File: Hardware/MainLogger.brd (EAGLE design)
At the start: 90 x 70 mm, 225 parts, among them J2 GEMS_POWER_PLUGINPUT, J4 U.FL, Q1 DMG3404, Q2 MOSFET_PCH-DMP3036SFG, Q3 MOSFET_PCH-DMP3036SFG, Q4 DMG3404, Q5 NX2301P, U1 MMC5633, U10 MXC6655, U11 FXMAR2102UMLP, U12 MCP79412SOIC, U13 SN74LVC1G17DCK, U14 FXMAR2102UMLP, U15 SN74AUP1G08DCK, U16 TPL5010DDC, U17 TPL5010DDC, U18 HALL_EFFECT_SI7201, U19 LP59073.3VYKE, U2 PAC1934QFN, U20 VEML3328, U21 MIC22602, U23 MB85RC, U24 SN74AUP3G34DCU, U25 SIP32431TDFN, U26 PAC1934QFN, U27 MCP23018QFN, U28 PCA9634QFN, U3 LTC4412S6, U4 BQ25616, U5 MCP23018QFN, U6 MAX-M8W, U7 B_SERIES_M.2EKEY_3042, U8 TCR2LE31ESV, U9 TPS61282D

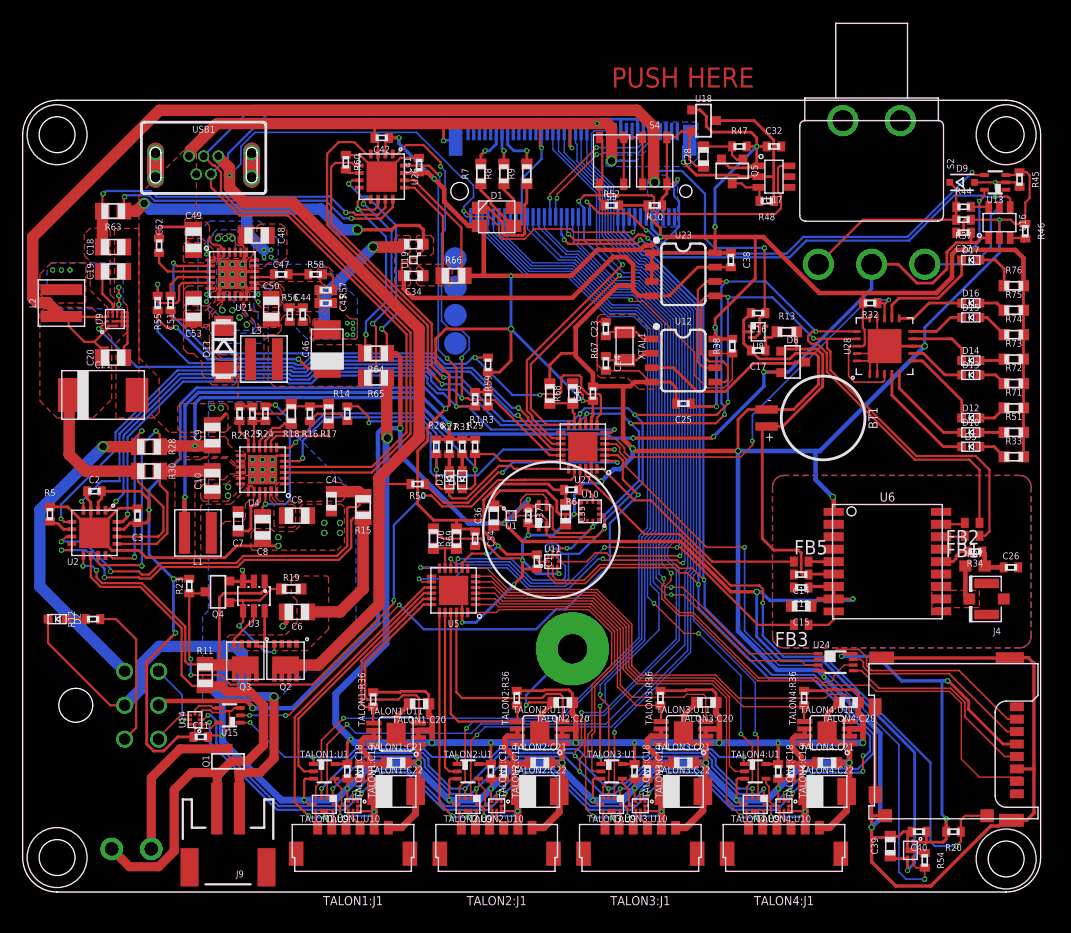
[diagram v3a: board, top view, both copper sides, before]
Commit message: Layout and cleanup complete, review required
Also add test points
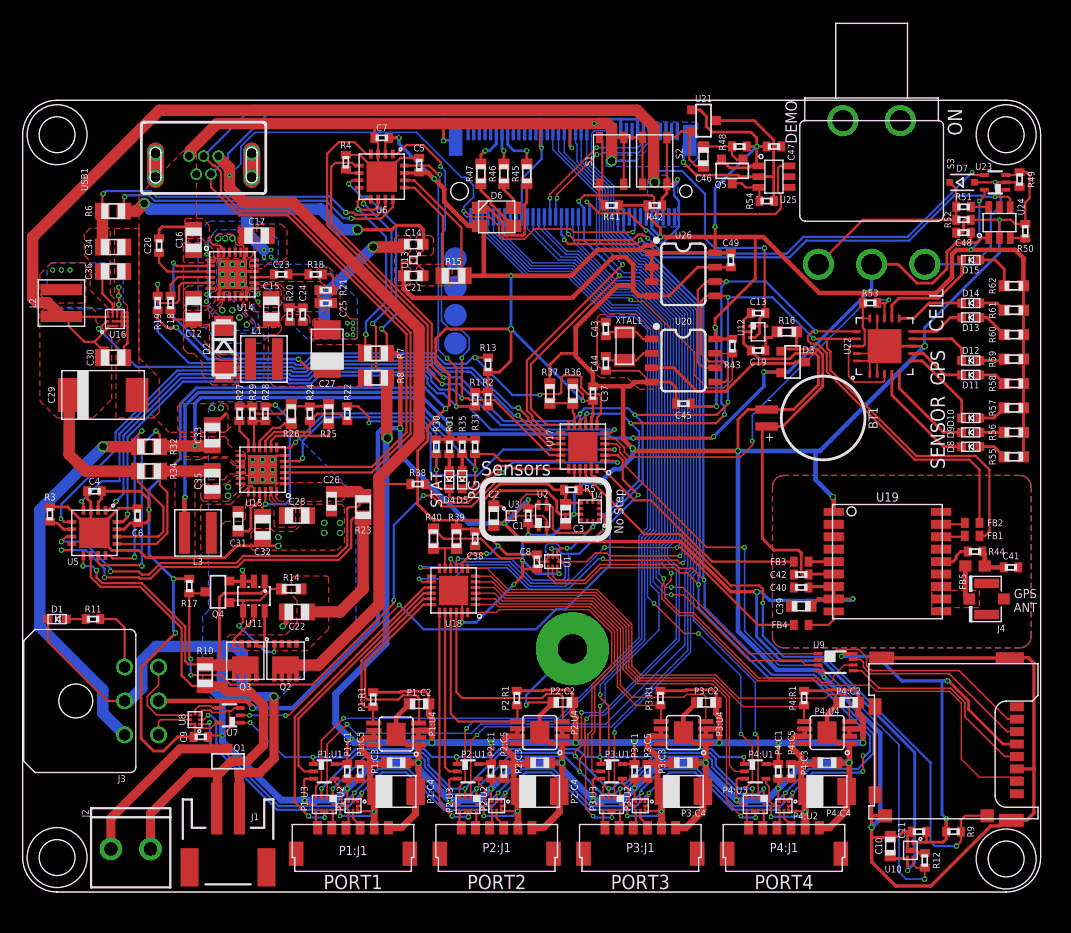
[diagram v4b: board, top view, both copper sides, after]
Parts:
- removed C50: 22uF, bschulz_passives:C0805
- removed C51: 1nF, bschulz_passives:C0402
- removed C52: 10nF, bschulz_passives:C0402
- removed C54: 0.1uF, bschulz_passives:C0402
- removed D16, D17: LED0603, bschulz:LED_0603
- removed FB7: 30Ω/1.8A, SparkFun-Coils:0603
- removed J9: (no value), bschulz:JST-2-SMD
- removed R63, R64, R65: 2m, bschulz_passives:R0805
- removed R66: 10m, bschulz_passives:R0805
- removed R67: (no value), bschulz_passives:R0603
- removed R71, R72, R73, R74: 220R, bschulz_passives:R0603
- removed S4: BUTTON4.2X3.2, bschulz:SWITCH_4.2X3.2
- removed U27: MCP23018QFN, bschulz:QFN24
- added $3_178_$_2021-10-08_21-38-43: B_SERIES_M.2EKEY_3042, Particle-Devices:PARTICLE_M.2EKEY
- added C22: 10uF, bschulz_passives:C0805
- added C29: 220uF, bschulz_passives:C2917
- added C30: 1.5uF, bschulz_passives:C0805
- added C31: 47nF, bschulz_passives:C0603
- added D7: BAT54WS, bschulz:SOD323-R
- added D8: LED0603, bschulz:LED_0603
- added FB4: (no value), bschulz:R0402
- added J3: GEMS_POWER_PLUGINPUT, bschulz:2X3_MICROFIT_RT
- added R2, R49: 1M, bschulz_passives:R0402
- added R22, R4: 0R, bschulz_passives:R0402
- added R35, R41, R42: 10k, bschulz_passives:R0402
- added R43, R53: 100k, bschulz_passives:R0402
- added S1: BUTTON4.2X3.2, bschulz:SWITCH_4.2X3.2
- C10: value 10uF -> 1uF; device bschulz_passives:C0805 -> bschulz_passives:C0603
- C14: value 0.1uF -> 1uF; device bschulz_passives:C0402 -> bschulz_passives:C0603
- C15: value 1uF -> 22uF; device bschulz_passives:C0603 -> bschulz_passives:C0805
- C16, C17: value 0.1uF -> 22uF; device bschulz_passives:C0402 -> bschulz_passives:C0805
- C18: value 10uF -> 1nF; device bschulz_passives:C0805 -> bschulz_passives:C0402
- C19, C5, C6, C9: value 10uF -> 0.1uF; device bschulz_passives:C0805 -> bschulz_passives:C0402
- C2, C3: value 0.1uF -> 2.2uF; device bschulz_passives:C0402 -> bschulz_passives:C0603
- C20: value 1.5uF -> 10nF; device bschulz_passives:C0805 -> bschulz_passives:C0402
- C21: value 220uF -> 1uF; device bschulz_passives:C2917 -> bschulz_passives:C0603
- C23: value 9pF -> 39pF
- C24: value 9pF -> 10nF
- C25: value 0.1uF -> 100pF
- C26: value 47pF -> 1uF; device bschulz_passives:C0402 -> bschulz_passives:C0603
- C27: value 0.1uF -> 100uF; device bschulz_passives:C0402 -> bschulz_passives:C1411_TANT
- C28, C33, C34: value 1uF -> 10uF; device bschulz_passives:C0603 -> bschulz_passives:C0805
- C32: value 0.1uF -> 4.7uF; device bschulz_passives:C0402 -> bschulz_passives:C0805
- C35, C36: value 2.2uF -> 10uF; device bschulz_passives:C0603 -> bschulz_passives:C0805
- C4: value 1uF -> 0.1uF; device bschulz_passives:C0603 -> bschulz_passives:C0402
- C41: value 0.1uF -> 47pF
- C43: value 0.1uF -> 9pF
- C44: value 10nF -> 9pF
- C45: value 100pF -> 0.1uF
- C46: value 100uF -> 1uF; device bschulz_passives:C1411_TANT -> bschulz_passives:C0603
- C47: value 39pF -> 0.1uF
- C48, C49: value 22uF -> 0.1uF; device bschulz_passives:C0805 -> bschulz_passives:C0402
- C7: value 47nF -> 0.1uF; device bschulz_passives:C0603 -> bschulz_passives:C0402
- C8: value 4.7uF -> 0.1uF; device bschulz_passives:C0805 -> bschulz_passives:C0402
- D1: value CLVBA-FKA -> LED0603; device bschulz:CLVBA-FKA -> bschulz:LED_0603
- D11: value CDBA3100 -> LED0603; device bschulz:DO214AC -> bschulz:LED_0603
- D2: value LED0603 -> CDBA3100; device bschulz:LED_0603 -> bschulz:DO214AC
- D3: value LED0603 -> BAT54C; device bschulz:LED_0603 -> bschulz:SOT23-3
- D6: value BAT54C -> CLVBA-FKA; device bschulz:SOT23-3 -> bschulz:CLVBA-FKA
- D9: value BAT54WS -> LED0603; device bschulz:SOD323-R -> bschulz:LED_0603
- FB5: value (none) -> 30Ω/1.8A; device bschulz:R0402 -> SparkFun-Coils:0603
- J1: device bschulz:SCREWTERMINAL-3.5MM-2_ROUND_RESTRICT -> bschulz:JST-2-SMD
- J2: value GEMS_POWER_PLUGINPUT -> (none); device bschulz:2X3_MICROFIT_RT -> bschulz:SCREWTERMINAL-3.5MM-2_ROUND_RESTRICT
- L1: value 1uH -> 1uF
- L3: value 1uF -> 1uH
- R10, R6: value 10k -> 2m; device bschulz_passives:R0402 -> bschulz_passives:R0805
- R11: value 2m -> 1k; device bschulz_passives:R0805 -> bschulz_passives:R0402
- R12: value 1k -> 100k
- R13: value 1k -> 100k; device bschulz_passives:R0603 -> bschulz_passives:R0402
- R14: value 0R -> 470k; device bschulz_passives:R0402 -> bschulz_passives:R0603
- R15: value 2m -> 10m
- R16: value 1M -> 1k; device bschulz_passives:R0402 -> bschulz_passives:R0603
- R17: value 470R -> 1M; device bschulz_passives:R0603 -> bschulz_passives:R0402
- R18: value 220R -> 20k; device bschulz_passives:R0603 -> bschulz_passives:R0402
- R19: value 470k -> 100k; device bschulz_passives:R0603 -> bschulz_passives:R0402
- R20, R54: value 100k -> 10k
- R21: value 10k -> 2.7k
- R23: value 1M -> 2m; device bschulz_passives:R0402 -> bschulz_passives:R0805
- R24, R38: value 100k -> 1M
- R25: value 100k -> 470R; device bschulz_passives:R0402 -> bschulz_passives:R0603
- R26: value 1M -> 220R; device bschulz_passives:R0402 -> bschulz_passives:R0603
- R28: value 10m -> 100k; device bschulz_passives:R0805 -> bschulz_passives:R0402
- R29, R50: value 1M -> 100k
- R3: value 1M -> 0R
- R30: value 10m -> 1M; device bschulz_passives:R0805 -> bschulz_passives:R0402
- R32: value 100k -> 10m; device bschulz_passives:R0402 -> bschulz_passives:R0805
- R33: value 220R -> 1M; device bschulz_passives:R0603 -> bschulz_passives:R0402
- R34: value 10 -> 10m; device bschulz_passives:R0402 -> bschulz_passives:R0805
- R37: value 1M -> (none); device bschulz_passives:R0402 -> bschulz_passives:R0603
- R44: value 10k -> 10
- R45: value 1M -> 4.7k; device bschulz_passives:R0402 -> bschulz_passives:R0603
- R46, R47: value 100k -> 4.7k; device bschulz_passives:R0402 -> bschulz_passives:R0603
- R48: value 10k -> 100k
- R5: value 0R -> 10k
- R51: value 220R -> 10k; device bschulz_passives:R0603 -> bschulz_passives:R0402
- R52: value 10k -> 1M
- R55, R59: value 100k -> 220R; device bschulz_passives:R0402 -> bschulz_passives:R0603
- R56: value 10k -> 220R; device bschulz_passives:R0402 -> bschulz_passives:R0603
- R57: value 2.7k -> 220R; device bschulz_passives:R0402 -> bschulz_passives:R0603
- R58: value 20k -> 220R; device bschulz_passives:R0402 -> bschulz_passives:R0603
- R60: value 0R -> 220R; device bschulz_passives:R0402 -> bschulz_passives:R0603
- R7, R8: value 4.7k -> 2m; device bschulz_passives:R0603 -> bschulz_passives:R0805
- R9: value 4.7k -> 100k; device bschulz_passives:R0603 -> bschulz_passives:R0402
- S2: value SPDT7103K2CWA -> BUTTON4.2X3.2; device bschulz:7103K2CWA -> bschulz:SWITCH_4.2X3.2
- S3: value BUTTON4.2X3.2 -> SPDT7103K2CWA; device bschulz:SWITCH_4.2X3.2 -> bschulz:7103K2CWA
- U1: value MMC5633 -> FXMAR2102UMLP; device bschulz:BGA_4 -> bschulz:UQFN-8_1.4X1.2
- U10: value MXC6655 -> SIP32431TDFN; device bschulz:LGA-12_2X2 -> bschulz:TDFN_4
- U11: value FXMAR2102UMLP -> LTC4412S6; device bschulz:UQFN-8_1.4X1.2 -> bschulz:SOT23-6L
- U12: value MCP79412SOIC -> TCR2LE31ESV; device bschulz:SO08 -> bschulz:SOT-553
- U13: value SN74LVC1G17DCK -> LP59073.3VYKE; device bschulz:DCK_R-PDSO-G5 -> bschulz:YKE0004
- U14: value FXMAR2102UMLP -> MIC22602; device bschulz:UQFN-8_1.4X1.2 -> bschulz:QFN24_POWER
- U15: value SN74AUP1G08DCK -> BQ25616; device bschulz:DCK_R-PDSO-G5 -> bschulz:QFN24_POWER
- U16: value TPL5010DDC -> TPS61282D; device bschulz:DDC_R-PDSO-G6 -> bschulz:YFP0016
- U17: value TPL5010DDC -> MCP23018QFN; device bschulz:DDC_R-PDSO-G6 -> bschulz:QFN24
- U18: value HALL_EFFECT_SI7201 -> MCP23018QFN; device bschulz:SOT23-3 -> bschulz:QFN24
- U19: value LP59073.3VYKE -> MAX-M8W; device bschulz:YKE0004 -> bschulz:MAX-M8
- U2: value PAC1934QFN -> VEML3328; device bschulz:QFN16 -> bschulz:VEML6075
- U20: value VEML3328 -> MCP79412SOIC; device bschulz:VEML6075 -> bschulz:SO08
- U21: value MIC22602 -> HALL_EFFECT_SI7201; device bschulz:QFN24_POWER -> bschulz:SOT23-3
- U23: value MB85RC -> SN74LVC1G17DCK; device bschulz:SO08 -> bschulz:DCK_R-PDSO-G5
- U24: value SN74AUP3G34DCU -> TPL5010DDC; device bschulz:DCU_(R-PDSO-G8) -> bschulz:DDC_R-PDSO-G6
- U25: value SIP32431TDFN -> TPL5010DDC; device bschulz:TDFN_4 -> bschulz:DDC_R-PDSO-G6
- U26: value PAC1934QFN -> MB85RC; device bschulz:QFN16 -> bschulz:SO08
- U3: value LTC4412S6 -> MMC5633; device bschulz:SOT23-6L -> bschulz:BGA_4
- U4: value BQ25616 -> MXC6655; device bschulz:QFN24_POWER -> bschulz:LGA-12_2X2
- U5: value MCP23018QFN -> PAC1934QFN; device bschulz:QFN24 -> bschulz:QFN16
- U6: value MAX-M8W -> PAC1934QFN; device bschulz:MAX-M8 -> bschulz:QFN16
- U7: value B_SERIES_M.2EKEY_3042 -> SN74AUP1G08DCK; device Particle-Devices:PARTICLE_M.2EKEY -> bschulz:DCK_R-PDSO-G5
- U8: value TCR2LE31ESV -> FXMAR2102UMLP; device bschulz:SOT-553 -> bschulz:UQFN-8_1.4X1.2
- U9: value TPS61282D -> SN74AUP3G34DCU; device bschulz:YFP0016 -> bschulz:DCU_(R-PDSO-G8)
- moved U16 78.7 mm to (8.16, 50.7), turned to 90 degrees
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- renumbered C53 to C12, R68 to R36, R69 to R40, R70 to R39, R75 to R61, R76 to R62, SD2 to SD1, TALON1:C18 to P1:C1, TALON1:C19 to P1:C5, TALON1:C20 to P1:C2, TALON1:C21 to P1:C3, TALON1:C22 to P1:C4, TALON1:J1 to P1:J1, TALON1:R36 to P1:R1, TALON1:U1 to P1:U1, TALON1:U10 to P1:U2, TALON1:U11 to P1:U4, TALON1:U9 to P1:U3, TALON2:C18 to P2:C1, TALON2:C19 to P2:C5, TALON2:C20 to P2:C2, TALON2:C21 to P2:C3, TALON2:C22 to P2:C4, TALON2:J1 to P2:J1, TALON2:R36 to P2:R1, TALON2:U1 to P2:U1, TALON2:U10 to P2:U2, TALON2:U11 to P2:U4, TALON2:U9 to P2:U3, TALON3:C18 to P3:C1, TALON3:C19 to P3:C5, TALON3:C20 to P3:C2, TALON3:C21 to P3:C3, TALON3:C22 to P3:C4, TALON3:J1 to P3:J1, TALON3:R36 to P3:R1, TALON3:U1 to P3:U1, TALON3:U10 to P3:U2, TALON3:U11 to P3:U4, TALON3:U9 to P3:U3, TALON4:C18 to P4:C1, TALON4:C19 to P4:C5, TALON4:C20 to P4:C2, TALON4:C21 to P4:C3, TALON4:C22 to P4:C4, TALON4:J1 to P4:J1, TALON4:R36 to P4:R1, TALON4:U1 to P4:U1, TALON4:U10 to P4:U2, TALON4:U11 to P4:U4, TALON4:U9 to P4:U3, U28 to U22
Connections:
- net TALON1:3V3_TALON renamed P1:3V3_TALON
- net TALON1:I2C_EN_LOCAL renamed P1:I2C_EN_LOCAL
- net TALON1:RX_TALON renamed P1:RX_TALON
- net TALON1:SCL_EXT renamed P1:SCL_EXT
- net TALON1:SDA_EXT renamed P1:SDA_EXT
- net TALON1:TX_TALON renamed P1:TX_TALON
- net TALON2:3V3_TALON renamed P2:3V3_TALON
- net TALON2:I2C_EN_LOCAL renamed P2:I2C_EN_LOCAL
- net TALON2:RX_TALON renamed P2:RX_TALON
- net TALON2:SCL_EXT renamed P2:SCL_EXT
- net TALON2:SDA_EXT renamed P2:SDA_EXT
- net TALON2:TX_TALON renamed P2:TX_TALON
- net TALON3:3V3_TALON renamed P3:3V3_TALON
- net TALON3:I2C_EN_LOCAL renamed P3:I2C_EN_LOCAL
- net TALON3:RX_TALON renamed P3:RX_TALON
- net TALON3:SCL_EXT renamed P3:SCL_EXT
- net TALON3:SDA_EXT renamed P3:SDA_EXT
- net TALON3:TX_TALON renamed P3:TX_TALON
- net TALON4:3V3_TALON renamed P4:3V3_TALON
- net TALON4:I2C_EN_LOCAL renamed P4:I2C_EN_LOCAL
- net TALON4:RX_TALON renamed P4:RX_TALON
- net TALON4:SCL_EXT renamed P4:SCL_EXT
- net TALON4:SDA_EXT renamed P4:SDA_EXT
- net TALON4:TX_TALON renamed P4:TX_TALON
- removed net N$20 (its old number): D3.ANODE, R27.1
- new net N$18: D5.ANODE, R35.1
- net !CE: now also R22.1, U17.3; no longer R14.1, U27.3
- net !CHG_PG: now also D5.CATHODE, R33.1, U15.7, U17.18; no longer D4.CATHODE, R29.1, U27.18, U4.7
- net !MODE: now also $3_178_$_2021-10-08_21-38-43.32, C46.1, R42.1, S2.1, S2.2, U21.2; no longer C28.1, R10.1, S4.1, S4.2, U18.2, U7.32
- net !RESET: now also $3_178_$_2021-10-08_21-38-43.34, FB4.2, R41.1, S1.1, S1.2, U17.12, U18.12, U25.6; no longer FB3.2, R52.1, S3.1, S3.2, U17.6, U27.12, U5.12, U7.34
- net !TALON1_FAULT: now also U18.17; no longer U5.17
- net !TALON2_FAULT: now also U18.21; no longer U5.21
- net !TALON3_FAULT: now also U18.2; no longer U5.2
- net !TALON4_FAULT: now also U18.6; no longer U5.6
- net 3V3_AUX: now also C1.1, C10.1, C2.1, C40.1, J3.5, R7.1, U10.3, U19.7, U19.8, U2.4, U3.B1; no longer C13.1, C15.1, C36.1, C37.1, J2.5, R64.1, U1.B1, U20.4, U25.3, U26.7, U6.8
- net 3V3_AUX_EN: now also R13.1, U14.2, U17.7; no longer R59.1, U21.2, U27.7
- net 3V3_AUX_PG: now also R19.1, U14.5, U17.15; no longer R55.1, U21.5, U27.15
- net 3V3_BULK: now also R8.1, U6.9; no longer R65.1, U26.9
- net 3V3_BULK+: now also C24.1, C27.ANODE, L1.P$2, R19.2, R20.2, R7.2, R8.2, U6.10, U6.8; no longer C44.1, C46.ANODE, L3.P$2, R55.2, R56.2, R64.2, R65.2, U26.10, U26.8
- net 3V3_CORE: now also $3_178_$_2021-10-08_21-38-43.10, $3_178_$_2021-10-08_21-38-43.12, C37.1, C4.1, C45.1, C47.1, C49.1, C5.1, C6.1, C7.1, C8.1, C9.1, D6.2, R13.2, R15.2, R17.2, R2.2, R41.2, R42.2, R43.2, R48.2, R5.2, R53.2, R55.2, R56.2, R57.2, R58.2, R60.2, U1.1, U1.8, U17.8, U18.8, U20.8, U21.1, U23.5, U25.1, U26.1, U26.3, U26.8, U4.7, U5.15, U5.2, U6.14, U6.15, U6.2, U7.5, U8.1, U8.8; no longer C1.1, C11.1, C2.1, C25.1, C32.1, C35.1, C41.1, C42.1, C43.1, C54.1, D1.2, R10.2, R23.2, R3.2, R32.2, R33.2, R38.2, R47.2, R51.2, R52.2, R6.2, R66.2, R71.2, R72.2, R73.2, R74.2, U10.7, U11.1, U11.8, U12.8, U13.5, U14.1, U14.8, U15.5, U17.1, U18.1, U2.15, U2.2, U23.1, U23.2, U23.3, U23.8, U26.14, U26.15, U27.8, U5.8, U7.10, U7.12
- net 3V3_CORE+: now also C21.1, R15.1, U13.A2, U6.13; no longer C34.1, R66.1, U19.A2, U26.13
- net 3V3_SD: now also C11.1, R9.2, U10.1, U9.8; no longer C40.1, R20.2, U24.8, U25.1
- net 3V3_SD_EN: now also R12.2, U10.4, U17.4; no longer R54.2, U25.4, U27.4
- net ACCEL_INT: now also R5.1, U17.21, U4.5; no longer R6.1, U10.5, U27.21
- net ANT_VCC: now also C41.1, FB5.2, R44.1; no longer C26.1, FB7.2, R34.1
- net BAT: now also J3.1, R32.2, U5.12; no longer J2.1, R28.2, U2.12
- net BAT_CHG: now also C33.1, C48.1, D3.2, R32.1, S3.2, U15.13, U15.14, U24.1, U5.11; no longer C27.1, C9.1, D6.2, R28.1, S2.2, U16.1, U2.11, U4.13, U4.14
- net BCKP_GPS: now also C42.1, D3.1, R16.2, U19.6; no longer C14.1, D6.1, R13.2, U6.6
- net BCKP_RTC: now also D3.3, U20.3; no longer D6.3, U12.3
- net BTST: now also C31.2, U15.21; no longer C7.2, U4.21
- net CHG_SOURCE: now also R17.1, U17.20; no longer R23.1, U27.20
- net CHG_STAT: now also D4.CATHODE, R30.1, U15.5, U17.19; no longer D3.CATHODE, R26.1, U27.19, U4.5
- net COMP: now also C23.1, U14.15; no longer C47.1, U21.15
- net CSA_ALERT: now also R2.1, U17.17, U5.1, U6.1; no longer R3.1, U2.1, U26.1, U27.17
- net CSA_EN: now also U17.6, U5.16, U6.16; no longer U2.16, U26.16, U27.6
- net D+: now also $3_178_$_2021-10-08_21-38-43.11, $3_178_$_2021-10-08_21-38-43.44, U15.3; no longer U4.3, U7.11, U7.44
- net D-: now also $3_178_$_2021-10-08_21-38-43.13, $3_178_$_2021-10-08_21-38-43.46, U15.4; no longer U4.4, U7.13, U7.46
- net DELAY: now also C20.1, U14.3; no longer C52.1, U21.3
- net EN_MAIN: now also R51.2, U24.6; no longer R44.2, U16.6
- net FAULT_BUS: now also D1.ANODE, R11.2; no longer D2.ANODE, R12.2
- net FB: now also C24.2, C25.1, R20.1, R21.2, U14.14; no longer C44.2, C45.1, R56.1, R57.2, U21.14
- net GND: now also $3_178_$_2021-10-08_21-38-43.1, $3_178_$_2021-10-08_21-38-43.15, $3_178_$_2021-10-08_21-38-43.21, $3_178_$_2021-10-08_21-38-43.3, $3_178_$_2021-10-08_21-38-43.39, $3_178_$_2021-10-08_21-38-43.49, $3_178_$_2021-10-08_21-38-43.5, $3_178_$_2021-10-08_21-38-43.56, $3_178_$_2021-10-08_21-38-43.7, $3_178_$_2021-10-08_21-38-43.76, $3_178_$_2021-10-08_21-38-43.77, $3_178_$_2021-10-08_21-38-43.9, $3_178_$_2021-10-08_21-38-43.GND, C21.2, C22.2, C27.CATHODE, C28.2, C29.-, C30.2, C44.2, C47.2, C7.2, D1.CATHODE, D2.A, J1.1, J3.2, R12.1, R21.1, R24.1, R26.1, R27.2, R29.1, R3.1, R4.1, R49.1, R50.1, R52.1, S1.3, S1.4, S2.3, S2.4, U1.4, U10.2, U10.EP, U11.2, U11.3, U12.2, U13.B2, U14.12, U14.16, U14.19, U14.24, U14.7, U14.EP, U14.EP@1, U14.EP@2, U14.EP@3, U14.EP@4, U14.EP@5, U14.EP@6, U14.EP@7, U14.EP@8, U14.EP@9, U15.17, U15.18, U15.6, U15.EP, U15.EP@1, U15.EP@2, U15.EP@3, U15.EP@4, U15.EP@5, U15.EP@6, U15.EP@7, U15.EP@8, U15.EP@9, U16.B2, U16.C2, U16.D1, U16.D2, U16.D3, U16.D4, U17.23, U17.EP, U18.23, U18.EP, U19.1, U19.10, U19.12, U19.15, U2.1, U20.4, U21.3, U23.3, U24.2, U26.4, U26.7, U3.A1, U4.9, U5.3, U6.3, U6.EP, U8.4, U9.4; no longer C21.-, C23.2, C24.2, C27.2, C46.CATHODE, C50.2, C51.2, C52.2, C54.2, D11.A, D2.CATHODE, J2.2, J9.1, R16.1, R17.1, R21.2, R45.1, R46.1, R48.1, R5.1, R57.1, R58.1, R60.1, R67.1, S3.3, S3.4, S4.3, S4.4, U1.A1, U10.9, U11.4, U12.4, U13.3, U14.4, U15.3, U16.2, U17.2, U18.3, U19.B2, U2.3, U2.EP, U20.1, U21.12, U21.16, U21.19, U21.24, U21.7, U21.EP, U21.EP@1, U21.EP@2, U21.EP@3, U21.EP@4, U21.EP@5, U21.EP@6, U21.EP@7, U21.EP@8, U21.EP@9, U23.4, U23.7, U24.4, U25.EP, U26.3, U26.EP, U27.23, U27.EP, U3.2, U3.3, U4.17, U4.18, U4.6, U4.EP, U4.EP@1, U4.EP@2, U4.EP@3, U4.EP@4, U4.EP@5, U4.EP@6, U4.EP@7, U4.EP@8, U4.EP@9, U5.23, U6.1, U6.10, U6.12, U6.15, U7.1, U7.15, U7.21, U7.39, U7.49, U7.5, U7.56, U7.7, U7.76, U7.77, U7.9, U7.GND, U8.2, U9.B2, U9.C2, U9.D1, U9.D2, U9.D3, U9.D4
- net GPS_ANT: now also FB5.1, U19.11; no longer FB7.1, U6.11
- net GPS_INT: now also FB3.1, U17.24; no longer FB5.1, U27.24
- net GPS_INT_CLEAN: now also FB3.2, U19.5; no longer FB5.2, U6.5
- net I2C_EXT_EN: now also U17.2, U7.2; no longer U15.2, U27.2
- net I2C_EXT_EN_OUT: now also U7.4, U8.5; no longer U14.5, U15.4
- net I2C_GLOBAL_EN: now also $3_178_$_2021-10-08_21-38-43.64, U7.1; no longer U15.1, U7.64
- net I2C_OB_EN: now also $3_178_$_2021-10-08_21-38-43.45, U1.5; no longer U11.5, U7.45
- net ICHG: now also R26.2, U15.10; no longer R18.2, U4.10
- net ILIM: now also R25.2, U15.8; no longer R17.2, U4.8
- net LED_BLUE: now also $3_178_$_2021-10-08_21-38-43.65, R47.2; no longer R7.2, U7.65
- net LED_EN: now also R53.1, U17.5; no longer R32.1, U27.5
- net LED_GREEN: now also $3_178_$_2021-10-08_21-38-43.63, R46.2; no longer R8.2, U7.63
- net LED_RED: now also $3_178_$_2021-10-08_21-38-43.61, R45.2; no longer R9.2, U7.61
- net MISO: now also $3_178_$_2021-10-08_21-38-43.50; no longer U7.50
- net MOSI: now also $3_178_$_2021-10-08_21-38-43.52, U9.1; no longer U24.1, U7.52
- net MOSI_BUF: now also U9.7; no longer U24.7
- net N$1: now also R3.2, U5.6; no longer R5.2, U2.6
- net N$10: now also R22.2, R24.2, U15.9; no longer R14.2, R16.2, U4.9
- net N$12: now also D7.A, R49.2, S3.3, U23.2; no longer D9.A, R45.2, S2.3, U13.2
- net N$13: now also C46.2, R48.1; no longer C28.2, R47.1
- net N$15: now also R38.1, U17.1; no longer R50.1, U27.1
- net N$17: now also R4.2, U6.6; no longer R60.2, U26.6
- net N$21: now also D6.3, R47.1; no longer D1.3, R7.1
- net N$22: now also D6.4, R46.1; no longer D1.4, R8.1
- net N$23: now also D6.1, R45.1; no longer D1.1, R9.1
- net N$24: now also FB4.1, U19.9; no longer FB3.1, U6.9
- net N$25: now also J3.3, R11.1; no longer J2.3, R12.1
- net N$29: now also D7.C, R51.1, R52.2, S3.1; no longer D9.C, R37.2, R44.1, S2.1
- net N$3: now also C19.1, R16.1, U12.4; no longer C17.1, R13.1, U8.4
- net N$30: now also R50.2, U24.3; no longer R46.2, U16.3
- net N$32: now also R54.2, U25.3; no longer R48.2, U17.3
- net N$33: now also C23.2, R18.2; no longer C47.2, R58.2
- net N$35: now also U18.11; no longer U5.11
- net N$36: now also D8.CATHODE; no longer D5.CATHODE
- net N$37: now also D9.CATHODE; no longer D10.CATHODE
- net N$38: now also R37.2, U17.11; no longer R67.2, U27.11
- net N$39: now also D10.CATHODE; no longer D12.CATHODE
- net N$4: now also C43.1, U20.1; no longer C23.1, U12.1
- net N$40: now also D11.CATHODE; no longer D13.CATHODE
- net N$41: now also D12.CATHODE; no longer D14.CATHODE
- net N$42: now also D13.CATHODE; no longer D15.CATHODE
- net N$43: now also D14.CATHODE; no longer D16.CATHODE
- net N$44: now also D15.CATHODE; no longer D17.CATHODE
- net N$45: now also D8.ANODE, R55.1; no longer D5.ANODE, R33.1
- net N$46: now also D9.ANODE, R56.1; no longer D10.ANODE, R51.1
- net N$47: now also D10.ANODE, R57.1; no longer D12.ANODE, R71.1
- net N$48: now also D11.ANODE, R58.1; no longer D13.ANODE, R72.1
- net N$49: now also D12.ANODE, R59.1; no longer D14.ANODE, R73.1
- net N$5: now also U11.5; no longer U3.5
- net N$50: now also D13.ANODE, R60.1; no longer D15.ANODE, R74.1
- net N$51: now also D14.ANODE; no longer D16.ANODE
- net N$52: now also D15.ANODE; no longer D17.ANODE
- net N$7: now also C44.1, U20.2; no longer C24.1, U12.2
- net OB_INT: now also $3_178_$_2021-10-08_21-38-43.43, U17.14; no longer U27.14, U7.43
- net PMID: now also C28.1, U15.23; no longer C5.1, U4.23
- net RC: now also C18.1, U14.4; no longer C51.1, U21.4
- net REGN: now also C32.1, R28.2, U15.22; no longer C8.1, R24.2, U4.22
- net RTC_INT: now also $3_178_$_2021-10-08_21-38-43.62, R43.1, U20.7; no longer R38.1, U12.7, U7.62
- net RX: now also $3_178_$_2021-10-08_21-38-43.38; no longer U7.38
- net SCK: now also $3_178_$_2021-10-08_21-38-43.54, U9.3; no longer U24.3, U7.54
- net SCK_BUF: now also U9.5; no longer U24.5
- net SCL: now also $3_178_$_2021-10-08_21-38-43.20, U1.3, U8.3; no longer U11.3, U14.3, U7.20
- net SCL_EXT: now also J3.6, U8.6; no longer J2.6, U14.6
- net SCL_GPS: now also U19.17; no longer U6.17
- net SCL_OB: now also U1.6, U17.9, U18.9, U2.3, U20.6, U26.6, U3.A2, U4.12, U5.4, U6.4; no longer U1.A2, U10.12, U11.6, U12.6, U2.4, U20.3, U23.6, U26.4, U27.9, U5.9
- net SDA: now also $3_178_$_2021-10-08_21-38-43.22, U1.2, U8.2; no longer U11.2, U14.2, U7.22
- net SDA_EXT: now also J3.4, U8.7; no longer J2.4, U14.7
- net SDA_GPS: now also U19.16; no longer U6.16
- net SDA_OB: now also U1.7, U17.10, U18.10, U2.2, U20.5, U3.B2, U4.2, U5.5, U6.5; no longer U1.B2, U10.2, U11.7, U12.5, U2.5, U20.2, U23.5, U27.10, U5.10
- net SD_CD: now also R9.1, U17.22; no longer R20.1, U27.22
- net SD_CS: now also $3_178_$_2021-10-08_21-38-43.48, U9.6; no longer U24.6, U7.48
- net SD_CS_BUF: now also U9.2; no longer U24.2
- net SIM_VCC: now also $3_178_$_2021-10-08_21-38-43.67; no longer U7.67
- net SOLAR+: now also J1.2, J2.1, R10.1, U5.10; no longer J1.1, J9.2, R11.1, U2.10
- net SOLAR-: now also J2.2; no longer J1.2
- net ST_CORE: now also R14.1, U11.4; no longer R19.1, U3.4
- net SW: now also C31.1, L3.P$1, U15.19, U15.20; no longer C7.1, L1.P$1, U4.19, U4.20
- net SW1: now also D2.C, L1.P$1, U14.10, U14.11, U14.20, U14.21, U14.22, U14.23, U14.8, U14.9; no longer D11.C, L3.P$1, U21.10, U21.11, U21.20, U21.21, U21.22, U21.23, U21.8, U21.9
- net SW2: now also U16.C3, U16.C4; no longer U9.C3, U9.C4
- net SYS: now also $3_178_$_2021-10-08_21-38-43.2, $3_178_$_2021-10-08_21-38-43.4, $3_178_$_2021-10-08_21-38-43.6, $3_178_$_2021-10-08_21-38-43.8, C13.1, C29.+, C30.1, R34.2, U12.1, U12.3, U16.A1, U16.A3, U16.A4, U16.B1, U16.C1, U5.14; no longer C16.1, C20.1, C21.+, R30.2, U2.14, U7.2, U7.4, U7.6, U7.8, U8.1, U8.3, U9.A1, U9.A3, U9.A4, U9.B1, U9.C1
- net SYSCORE: now also C35.1, L3.P$2, R30.2, R33.2, R34.1, R35.2, U15.15, U15.16, U5.13; no longer C10.1, L1.P$2, R26.2, R27.2, R29.2, R30.1, U2.13, U4.15, U4.16
- net TALON1_EN: now also U18.18; no longer U5.18
- net TALON1_GPIOA: now also $3_178_$_2021-10-08_21-38-43.37; no longer U7.37
- net TALON1_GPIOB: now also $3_178_$_2021-10-08_21-38-43.72; no longer U7.72
- net TALON1_I2C_EN: now also U18.16; no longer U5.16
- net TALON1_SEL: now also U18.15; no longer U5.15
- net TALON2_EN: now also U18.22; no longer U5.22
- net TALON2_GPIOA: now also $3_178_$_2021-10-08_21-38-43.35; no longer U7.35
- net TALON2_GPIOB: now also $3_178_$_2021-10-08_21-38-43.70; no longer U7.70
- net TALON2_I2C_EN: now also U18.20; no longer U5.20
- net TALON2_SEL: now also U18.19; no longer U5.19
- net TALON3_EN: now also U18.3; no longer U5.3
- net TALON3_GPIOA: now also $3_178_$_2021-10-08_21-38-43.33; no longer U7.33
- net TALON3_GPIOB: now also $3_178_$_2021-10-08_21-38-43.68; no longer U7.68
- net TALON3_I2C_EN: now also U18.1; no longer U5.1
- net TALON3_SEL: now also U18.24; no longer U5.24
- net TALON4_EN: now also U18.7; no longer U5.7
- net TALON4_GPIOA: now also $3_178_$_2021-10-08_21-38-43.23; no longer U7.23
- net TALON4_GPIOB: now also $3_178_$_2021-10-08_21-38-43.66; no longer U7.66
- net TALON4_I2C_EN: now also U18.5; no longer U5.5
- net TALON4_SEL: now also U18.4; no longer U5.4
- net TALON_INT: now also $3_178_$_2021-10-08_21-38-43.41, U18.14; no longer U5.14, U7.41
- net TEST: now also $3_178_$_2021-10-08_21-38-43.40, U23.4; no longer U13.4, U7.40
- net TS: now also R28.1, R29.2, U15.11; no longer R24.1, R25.2, U4.11
- net TX: now also $3_178_$_2021-10-08_21-38-43.36; no longer U7.36
- net VBULK: now also C14.1, C15.1, C16.1, C17.1, R6.1, U13.A1, U13.B1, U14.1, U14.13, U14.17, U14.18, U14.6, U6.12; no longer C33.1, C48.1, C49.1, C50.1, R63.1, U19.A1, U19.B1, U21.1, U21.13, U21.17, U21.18, U21.6, U26.12
- net VBULK+: now also C34.1, C36.1, R6.2, U16.B3, U16.B4, U6.11; no longer C18.1, C19.1, R63.2, U26.11, U9.B3, U9.B4
- net VBULK_PG: now also U16.A2, U17.16; no longer U27.16, U9.A2
- net VBUS: now also C26.1, R23.2, U15.1, U15.24, U5.7; no longer C4.1, R15.2, U2.7, U4.1, U4.24
- net VCC_RF: now also R44.2, U19.14; no longer R34.2, U6.14
- net VPRIME: now also C22.1, R14.2, R23.1, U11.6, U5.8; no longer C6.1, R15.1, R19.2, U2.8, U3.6
- net VSET: now also R27.1, U15.12; no longer R21.1, U4.12
- net VSOLAR: now also R10.2, U11.1, U5.9; no longer R11.2, U2.9, U3.1
- net VUSB: now also $3_178_$_2021-10-08_21-38-43.16, $3_178_$_2021-10-08_21-38-43.74, R38.2; no longer R50.2, U7.16, U7.74
- net WDT_DONE: now also $3_178_$_2021-10-08_21-38-43.42, U24.4; no longer U16.4, U7.42
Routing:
- net N$25: track 13.2 -> 5.94 mm
- net SOLAR+: track 53.2 -> 47.1 mm
- net BAT: track 44.1 -> 49.7 mm
- net SCL_EXT: track 3.72 -> 7.91 mm
- net SDA_EXT: track 5.98 -> 3.99 mm, vias 1 -> 0
- net SOLAR-: track 14.1 -> 15.6 mm
- net N$20 (its old number): track 1.47 -> 0.00 mm
- net N$18: track 0.00 -> 1.47 mm
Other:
- board text added: "!MODE"
- board text added: "!RST"
- board text added: "4V~13V"
- board text added: "CELL"
- board text added: "DEMO"
- board text added: "GEMS SENSING"
- board text added: "GPS"
- board text added: "GPS ANT"
- board text added: "No Step"
- board text added: "ON"
- board text added: "PORT1"
- board text added: "PORT2"
- board text added: "PORT3"
- board text added: "PORT4"
- board text added: "Project Kestrel v0.0 Bobby Schulz"
- board text added: "SENSOR"
- board text added: "Safe Mode"
- board text added: "Sensors"
- board text added: "TOUGH COMPETENT"
- board text removed: "-\"
- board text removed: "BATT IN"
- board text removed: "FAULT"
- board text removed: "POWER OUT"
- board text removed: "PUSH HERE"
- board text removed: "Project Yoshino Ext - v0.0B Bobby Schulz"
- board text removed: "Vin"

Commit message: Layout, gerbers, and BoM for v0.0 - sent to fab
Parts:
- added D16: RCLAMP3654, bschulz:DFN_6_1.6X1.6
- added R63, R64: 27R, bschulz_passives:R0402
- added TP1, TP2, TP3, TP4, TP5, TP6, TP7, TP8, TP9: TESTPOINTRCU, bschulz:TESTPOINT_0603
- C31: device bschulz_passives:C0603 -> bschulz_passives:C0402
- D1, D10, D15: value LED0603 -> LEDRED0603
- D11, D13, D4, D8: value LED0603 -> LEDGREEN0603
- D12, D14, D5, D9: value LED0603 -> LEDAMBER0603
- L1: value 1uF -> 1uH
- R25, R26: device bschulz_passives:R0603 -> bschulz_passives:R0402
- R36: value (none) -> 150k
- R37: value (none) -> 10k
- R39: value (none) -> 130k
- R40: value (none) -> 30k
- moved USB1 1.91 mm to (15.9, 66.2)
- renumbered $3_178_$_2021-10-08_21-38-43 to J5
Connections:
- new net D+_IN: D16.2, R63.2, USB1.3
- new net D-_IN: D16.1, R64.2, USB1.2
- net D+: now also R63.1; no longer USB1.3
- net D-: now also R64.1; no longer USB1.2
- net GND: now also D16.EP, TP1.1
- net OB_INT: now also TP7.1
- net RTC_INT: now also TP2.1
- net RX: now also TP9.1
- net SCL: now also TP6.1
- net SCL_OB: now also TP4.1
- net SDA: now also TP5.1
- net SDA_OB: now also TP3.1
- net TX: now also TP8.1
- net VUSB: now also D16.6
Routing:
- net GND: track 797.1 -> 814.2 mm
- net D-_IN: track 0.00 -> 8.57 mm
- net D+_IN: track 0.00 -> 7.03 mm
- net VUSB: track 118.2 -> 124.6 mm, vias 3 -> 4
- net D+: track 103.1 -> 98.7 mm, vias 2 -> 3
- net D-: track 99.9 -> 95.7 mm, vias 2 -> 3
- net TX: track 109.3 -> 112.7 mm, vias 6 -> 7
- net SCL: track 151.9 -> 154.9 mm
- net SYS: track 134.0 -> 136.7 mm
- net VBULK: track 62.6 -> 60.5 mm
- net SDA: track 152.7 -> 154.7 mm
- net OB_INT: track 34.7 -> 36.5 mm
- net RX: track 108.1 -> 109.7 mm, vias 6 -> 7
- net RTC_INT: track 32.6 -> 34.2 mm
- net SDA_OB: track 203.5 -> 204.9 mm
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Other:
- board text added: "GND"
- board text added: "OB_INT"
- board text added: "RTC_INT"
- board text added: "RX"
- board text added: "SCL"
- board text added: "SCL_OB"
- board text added: "SDA"
- board text added: "SDA_OB"
- board text added: "SN"
- board text added: "TX"
- board text removed: "!BYP"
- board text removed: "EN"
- board text removed: "SEL"
- board text removed: "Tosche TPS6128x v0.0 B. Schulz"
- board text removed: "Vout"

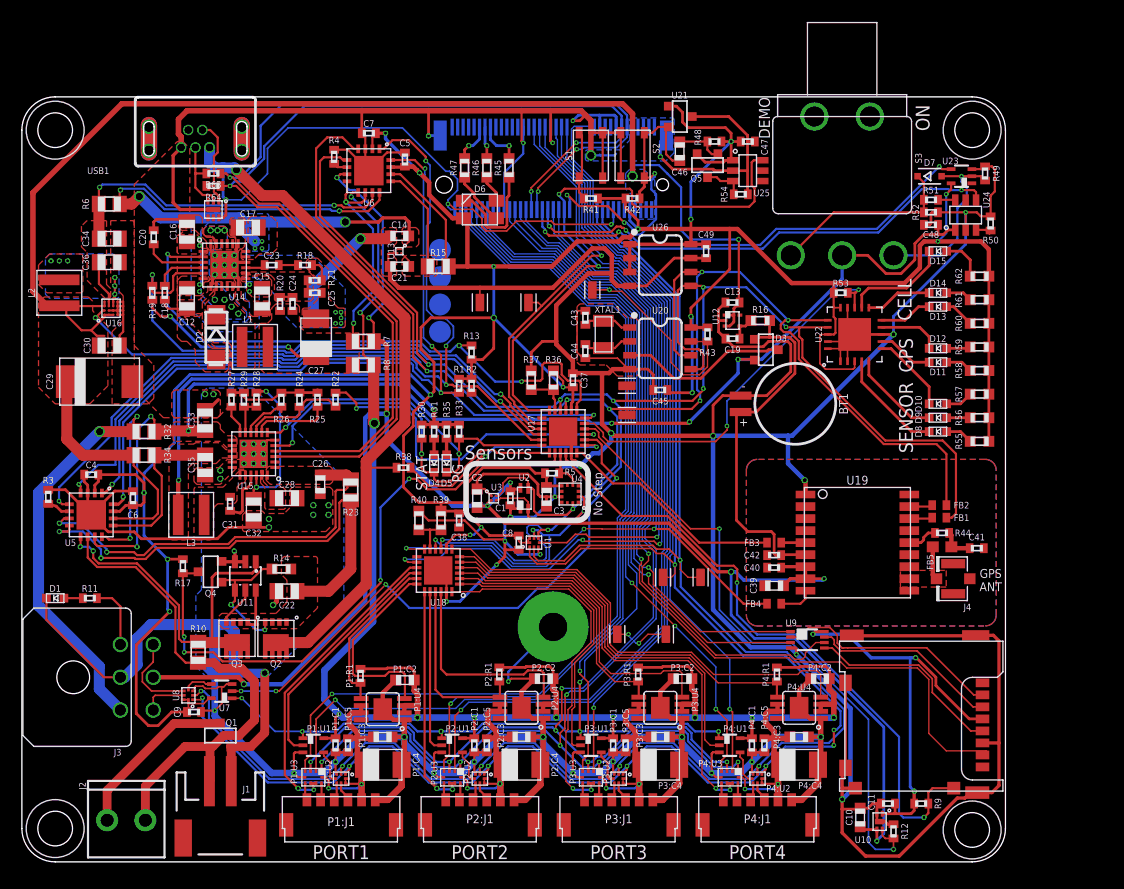
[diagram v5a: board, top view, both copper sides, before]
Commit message: v1.0 Update
Many fixes, see ECO and Github issues documentation, v1.0 sent to fab
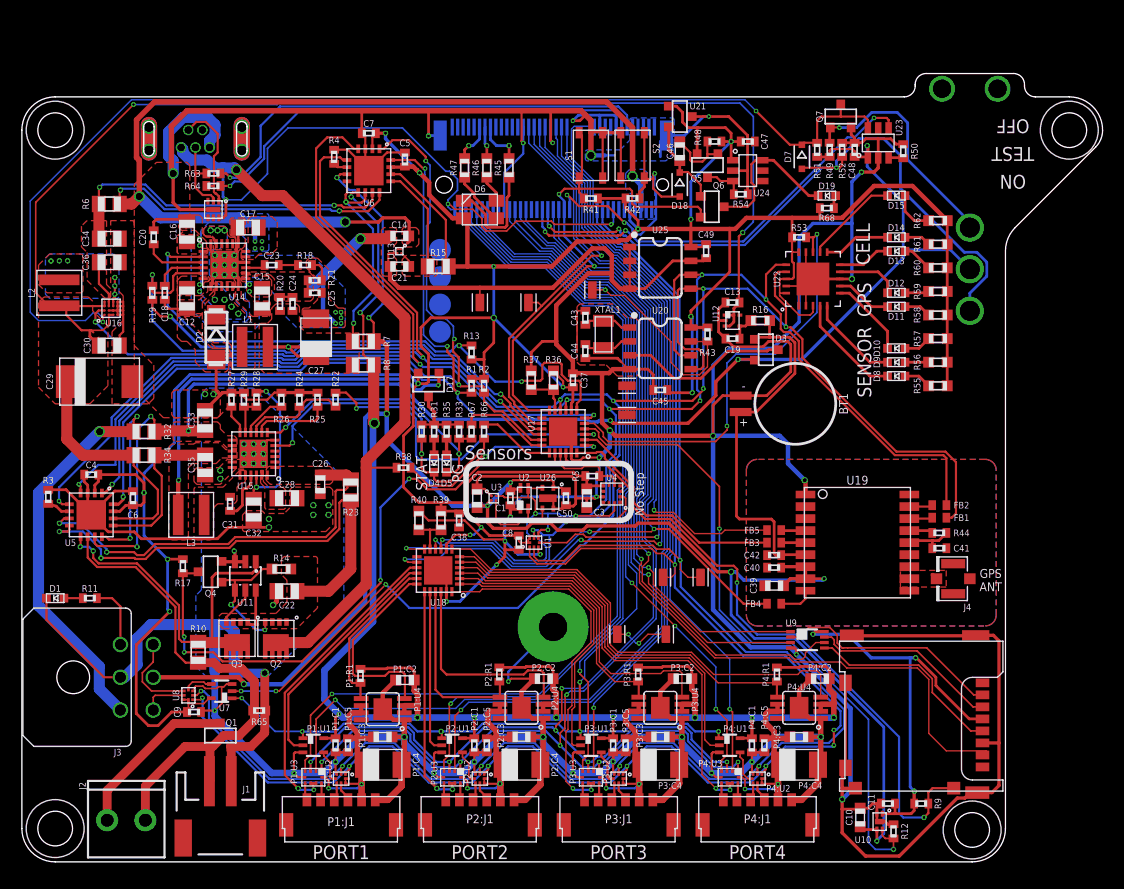
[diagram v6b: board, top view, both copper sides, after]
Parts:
- added C50: 0.1uF, bschulz_passives:C0402
- added D17: (no value), bschulz:SOT23-3
- added D18: BAT54WS, bschulz:SOD323-R
- added D19: LEDGREEN0603, bschulz:LED_0603
- added Q6: NX2301P, bschulz:SOT23-3
- added Q7: DMG3404, bschulz:SOT23-3
- added R65, R66, R67: 1M, bschulz_passives:R0402
- added R68: 10k, bschulz_passives:R0402
- FB5: value 30Ω/1.8A -> (none); device SparkFun-Coils:0603 -> bschulz:R0402
- J3: value GEMS_POWER_PLUGINPUT -> GEMS_POWER_PLUGINPUT_RT
- R51: value 10k -> 1M
- S3: value SPDT7103K2CWA -> SPDT7103K2CWAV2; device bschulz:7103K2CWA -> bschulz:7103K2CWAV2
- U23: value SN74LVC1G17DCK -> TPL5010DDC; device bschulz:DCK_R-PDSO-G5 -> bschulz:DDC_R-PDSO-G6
- U25: value TPL5010DDC -> MB85RC; device bschulz:DDC_R-PDSO-G6 -> bschulz:SO08
- U26: value MB85RC -> SHTC3DFN; device bschulz:SO08 -> bschulz:DFN_4_2X2
- moved U26 23.7 mm to (48.1, 33.3)
- moved U24 20.3 mm to (66.4, 63.2), turned to 270 degrees
- moved FB5 15.4 mm to (68.8, 30.4)
- moved R49 14.4 mm to (73.9, 65.2), turned to 90 degrees
- moved U25 12.0 mm to (58.4, 54.4)
- moved S3 12.0 mm to (86.7, 70.7), flipped to the bottom
- moved D7 11.8 mm to (71.4, 64.5), turned to 270 degrees
- moved R51 11.4 mm to (72.8, 65.2), turned to 270 degrees
- moved R50 10.4 mm to (80.6, 65.0)
- moved R52 9.94 mm to (75.1, 65.2), turned to 270 degrees
- moved C48 9.79 mm to (76.2, 65.2), turned to 90 degrees
- moved H1 8.89 mm to (95.8, 67.0)
- moved U23 8.21 mm to (78.4, 65.8), turned to 0 degrees
- moved R59 6.35 mm to (83.8, 52.2)
- moved U22 6.35 mm to (72.4, 53.3)
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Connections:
- removed net ANT_VCC: C41.1, FB5.2, R44.1
- removed net N$29: D7.C, R51.1, R52.2, S3.1
- new net N$11: C46.1, D18.C, Q6.1, U21.2
- new net N$14: D19.ANODE, R68.1
- new net N$6: R66.1, U17.19
- new net N$8: Q7.1, R49.2, S3.1
- new net N$9: R67.1, U17.18
- new net STAT_CORE: D17.3, R30.2, R31.2, R33.2, R35.2
- new net TIMEPULSE: FB5.1, J5.47
- new net TIMEPULSE_CLEAN: FB5.2, U19.4
- new net V_ANT: R44.2, U19.15
- net !CHG_PG: now also R67.2; no longer U17.18
- net !MODE: now also D18.A; no longer C46.1, U21.2
- net !RESET: now also Q6.2; no longer U25.6
- net 3V3_AUX: now also C50.1, U26.1
- net 3V3_CORE: now also D17.2, R68.2, U22.20, U24.1, U25.8; no longer U23.5, U25.1, U26.1, U26.2, U26.3, U26.8
- net BAT_CHG: now also R49.1, R51.2, U23.1; no longer U24.1
- net CHG_STAT: now also R66.2; no longer U17.19
- net D+: no longer J5.44, U15.3
- net D-: no longer J5.46, U15.4
- net EN_MAIN: now also D7.C, Q7.3, R51.1, U16.A1, U23.6; no longer R51.2, U24.6
- net GND: now also C50.2, Q7.2, R65.1, U23.2, U25.1, U25.3, U25.4, U25.7, U26.EP; no longer R49.1, U19.15, U22.20, U23.3, U26.7
- net GPS_ANT: no longer FB5.1
- net N$12: now also D19.CATHODE, Q6.3, U24.6; no longer D7.A, R49.2, S3.3, U23.2
- net N$30: now also U23.3; no longer U24.3
- net N$32: now also U24.3; no longer U25.3
- net SCL_OB: now also U25.6, U26.2; no longer U26.6
- net SDA_OB: now also U25.5, U26.3; no longer U26.5
- net SOLAR+: now also R65.2
- net SYS: no longer J5.2, J5.4, J5.6, J5.8, U16.A1
- net SYSCORE: now also D17.1; no longer R30.2, R31.2, R33.2, R35.2
- net TEST: now also D7.A, R52.2, S3.3; no longer U23.4
- net VBULK: now also J5.2, J5.4, J5.6, J5.8
- net VCC_RF: now also C41.1, R44.1; no longer R44.2
- net WDT_DONE: now also U23.4; no longer U24.4
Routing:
- net EN_MAIN: track 1.59 -> 105.2 mm, vias 0 -> 2
- net VBULK: track 60.5 -> 122.4 mm, vias 14 -> 15
- net D+: track 98.7 -> 43.2 mm, vias 3 -> 1
- net D-: track 95.7 -> 41.5 mm, vias 3 -> 1
- net TIMEPULSE: track 0.00 -> 52.1 mm, vias 0 -> 1
- net GND: track 814.2 -> 847.0 mm, vias 53 -> 54
- net N$8: track 0.00 -> 21.4 mm, vias 0 -> 1
- net TEST: track 42.5 -> 63.2 mm
- net 3V3_CORE: track 356.0 -> 336.8 mm, vias 18 -> 16
- net N$29: track 17.3 -> 0.00 mm
- net BAT_CHG: track 112.9 -> 128.3 mm
- net !RESET: track 125.6 -> 116.3 mm
- net SDA_OB: track 204.9 -> 214.0 mm
- net N$9: track 0.00 -> 8.31 mm
- net N$11: track 0.00 -> 8.09 mm
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- removed copper zone on layer 16, net SYS
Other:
- board size 90 x 70 mm -> 98.9 x 72.1 mm
- board text added: "MODE"
- board text added: "OFF"
- board text added: "PWR"
- board text added: "Project Kestrel v1.0 Bobby Schulz"
- board text added: "TEST"
- board text removed: "!MODE"
- board text removed: "DEMO"
- board text removed: "Project Kestrel v0.0 Bobby Schulz"
